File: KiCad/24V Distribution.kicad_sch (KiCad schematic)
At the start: 0 parts

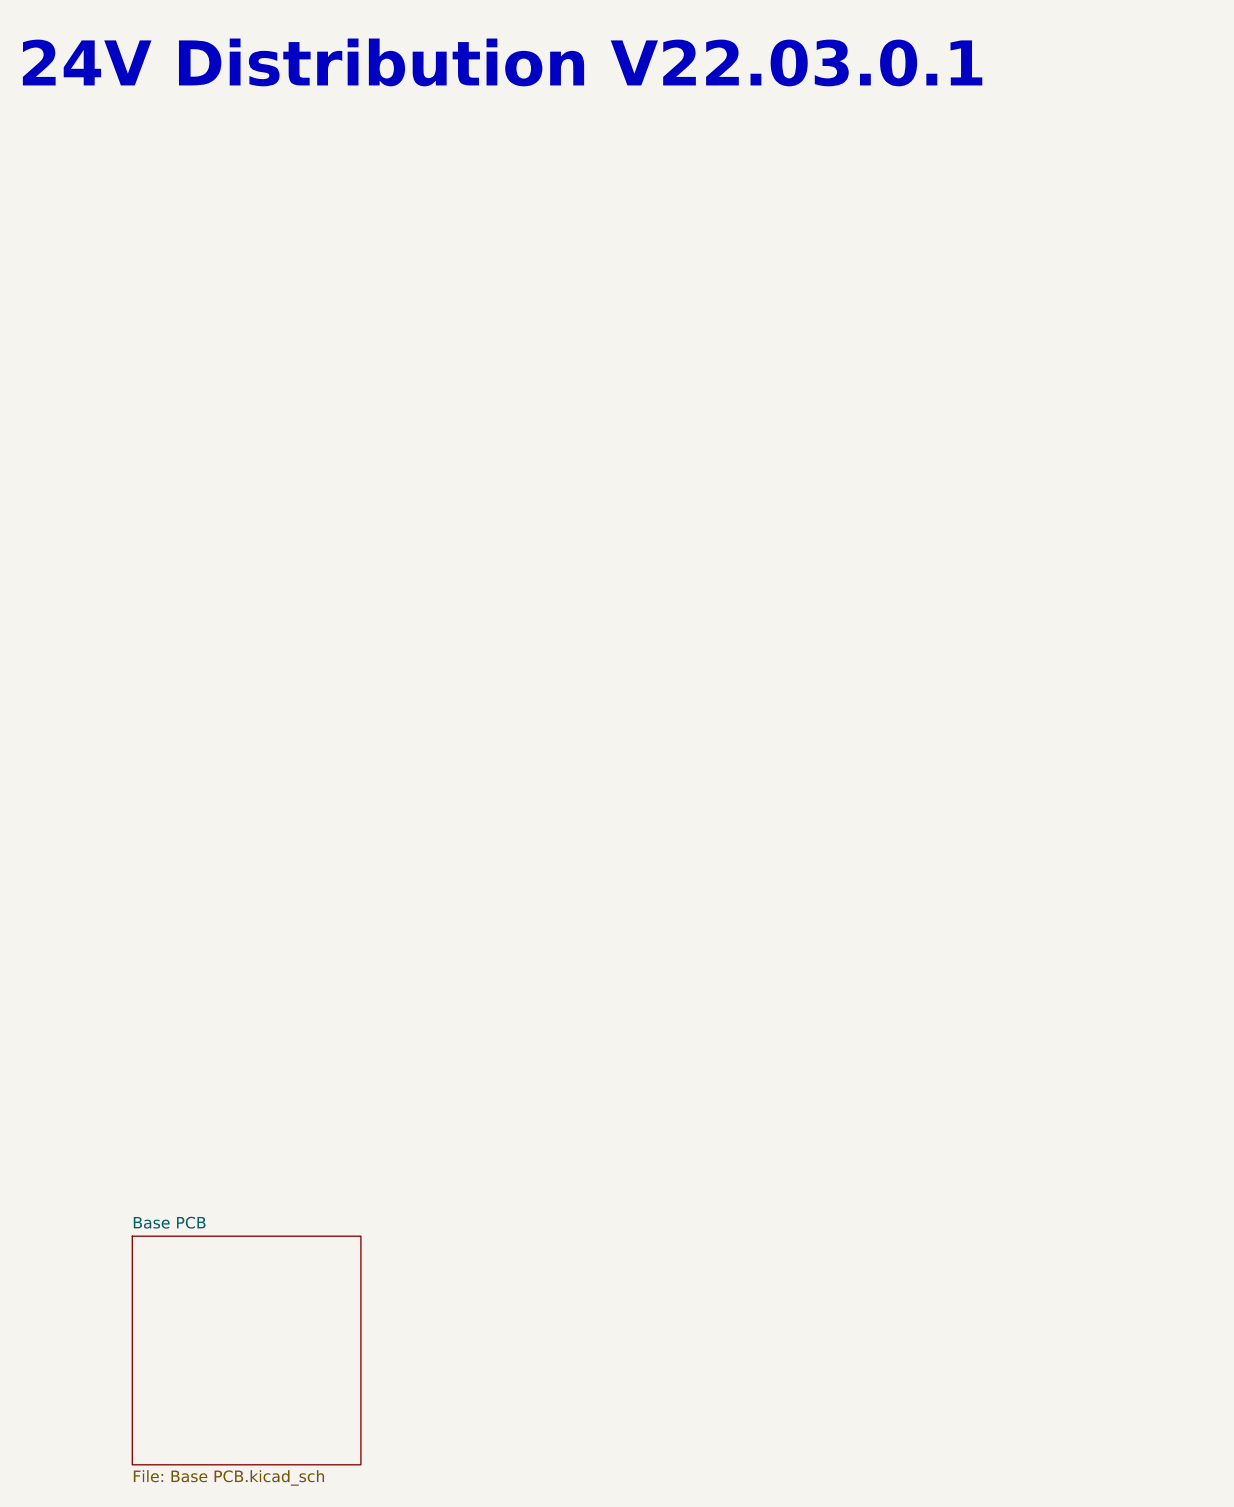
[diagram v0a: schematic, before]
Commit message: Updated PCB and schematic and changed datasheet
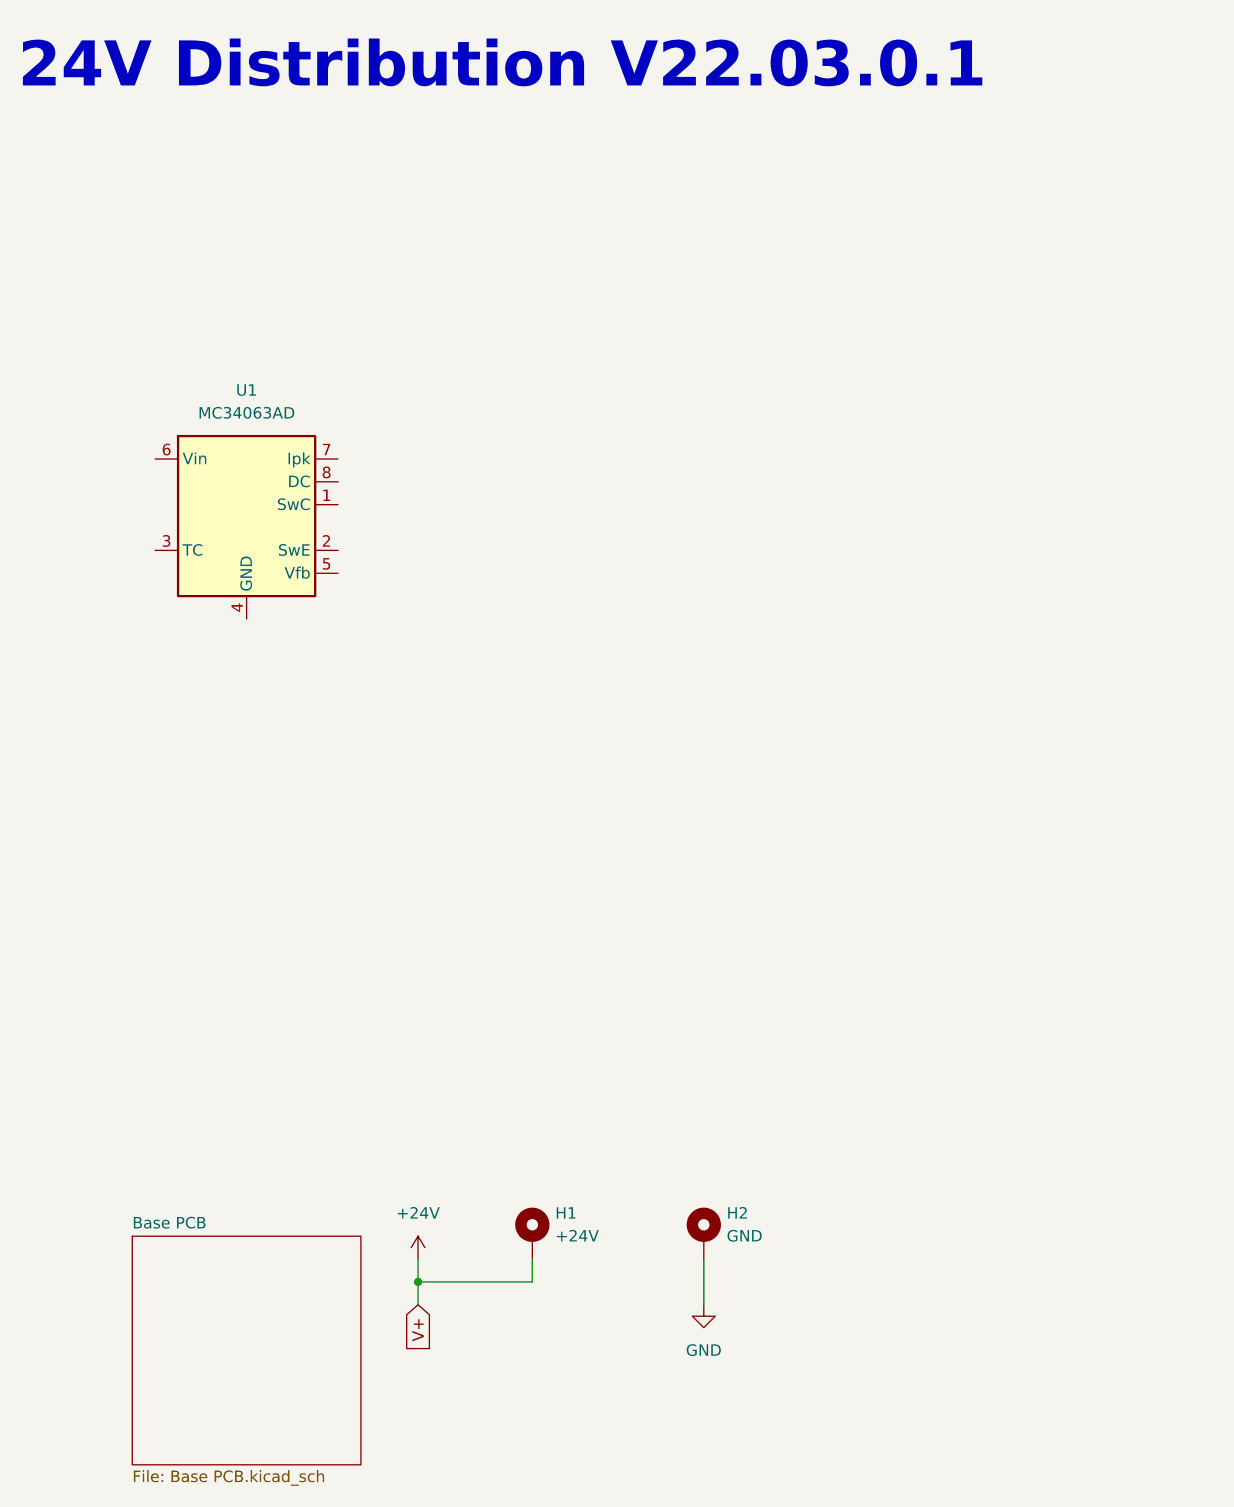
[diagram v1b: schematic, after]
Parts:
- added H1: +24V, MountingHole:MountingHole_4.3mm_M4_Pad_Via, symbol Mechanical:MountingHole_Pad
- added H2: GND, MountingHole:MountingHole_4.3mm_M4_Pad_Via, symbol Mechanical:MountingHole_Pad
- added U1: MC34063AD, Package_SO:SOIC-8_3.9x4.9mm_P1.27mm, symbol Regulator_Switching:MC34063AD
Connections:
- new net +24V: H1.1
- new net GND: H2.1
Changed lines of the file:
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@@
     (rev "V22.03.0.1")
+  )
+  (junction (at 69.85 157.48) (diameter 0) (color 0 0 0 0)
+  )
+  (wire (pts (xy 69.85 157.48) (xy 69.85 160.02))
+    (stroke (width 0) (type default) (color 0 0 0 0))
+  )
+  (wire (pts (xy 101.6 154.94) (xy 101.6 160.02))
+    (stroke (width 0) (type default) (color 0 0 0 0))
+  )
+  (wire (pts (xy 82.55 154.94) (xy 82.55 157.48))
+    (stroke (width 0) (type default) (color 0 0 0 0))
+  )
+  (wire (pts (xy 82.55 157.48) (xy 69.85 157.48))
+    (stroke (width 0) (type default) (color 0 0 0 0))
+  )
+  (wire (pts (xy 69.85 154.94) (xy 69.85 157.48))
+    (stroke (width 0) (type default) (color 0 0 0 0))
   )
   (text "24V Distribution V22.03.0.1" (at 25.4 25.4 0)
     (effects (font (size 5.0038 5.0038) (thickness 1.0008) bold) (justify left bottom))
+  )
+  (global_label "V+" (shape input) (at 69.85 160.02 270) (fields_autoplaced)
+    (effects (font (size 1.27 1.27)) (justify right))
+    (property "Intersheet References" "${INTERSHEET_REFS}" (id 0) (at 69.7706 165.0052 90)
+      (effects (font (size 1.27 1.27)) (justify right) hide)
+    )
+  )
+  (symbol (lib_id "Regulator_Switching:MC34063AD") (at 50.8 71.12 0) (unit 1)
+    (in_bom yes) (on_board yes) (fields_autoplaced)
+    (property "Reference" "U1" (id 0) (at 50.8 58.42 0))
+    (property "Value" "MC34063AD" (id 1) (at 50.8 60.96 0))
+    (property "Footprint" "Package_SO:SOIC-8_3.9x4.9mm_P1.27mm" (id 2) (at 52.07 82.55 0)
+      (effects (font (size 1.27 1.27)) (justify left) hide)
+    )
+    (property "Datasheet" "http://www.onsemi.com/pub_link/Collateral/MC34063A-D.PDF" (id 3) (at 63.5 73.66 0)
+      (effects (font (size 1.27 1.27)) hide)
+    )
+    (pin "1")
+    (pin "2")
+    (pin "3")
+    (pin "4")
+    (pin "5")
+    (pin "6")
+    (pin "7")
+    (pin "8")
+  )
+  (symbol (lib_id "Mechanical:MountingHole_Pad") (at 101.6 152.4 0) (unit 1)
+    (in_bom yes) (on_board yes) (fields_autoplaced)
+    (property "Reference" "H2" (id 0) (at 104.14 149.8599 0)
+      (effects (font (size 1.27 1.27)) (justify left))
+    )
+    (property "Value" "GND" (id 1) (at 104.14 152.3999 0)
+      (effects (font (size 1.27 1.27)) (justify left))
+    )
+    (property "Footprint" "MountingHole:MountingHole_4.3mm_M4_Pad_Via" (id 2) (at 101.6 152.4 0)
+      (effects (font (size 1.27 1.27)) hide)
+    )
+    (property "Datasheet" "~" (id 3) (at 101.6 152.4 0)
+      (effects (font (size 1.27 1.27)) hide)
+    )
+    (pin "1")
+  )
+  (symbol (lib_id "power:GND") (at 101.6 160.02 0) (unit 1)
+    (in_bom yes) (on_board yes) (fields_autoplaced)
+    (property "Reference" "#PWR0101" (id 0) (at 101.6 166.37 0)
+      (effects (font (size 1.27 1.27)) hide)
+    )
+    (property "Value" "GND" (id 1) (at 101.6 165.1 0))
+    (property "Footprint" "" (id 2) (at 101.6 160.02 0)
+      (effects (font (size 1.27 1.27)) hide)
+    )
+    (property "Datasheet" "" (id 3) (at 101.6 160.02 0)
+      (effects (font (size 1.27 1.27)) hide)
+    )
+    (pin "1")
+  )
+  (symbol (lib_id "power:+24V") (at 69.85 154.94 0) (unit 1)
+    (in_bom yes) (on_board yes) (fields_autoplaced)
+    (property "Reference" "#PWR0102" (id 0) (at 69.85 158.75 0)
+      (effects (font (size 1.27 1.27)) hide)
+    )
+    (property "Value" "+24V" (id 1) (at 69.85 149.86 0))
+    (property "Footprint" "" (id 2) (at 69.85 154.94 0)
+      (effects (font (size 1.27 1.27)) hide)
+    )
+    (property "Datasheet" "" (id 3) (at 69.85 154.94 0)
+      (effects (font (size 1.27 1.27)) hide)
+    )
+    (pin "1")
+  )
+  (symbol (lib_id "Mechanical:MountingHole_Pad") (at 82.55 152.4 0) (unit 1)
+    (in_bom yes) (on_board yes) (fields_autoplaced)
+    (property "Reference" "H1" (id 0) (at 85.09 149.8599 0)
+      (effects (font (size 1.27 1.27)) (justify left))
+    )
+    (property "Value" "+24V" (id 1) (at 85.09 152.3999 0)
+      (effects (font (size 1.27 1.27)) (justify left))
+    )
+    (property "Footprint" "MountingHole:MountingHole_4.3mm_M4_Pad_Via" (id 2) (at 82.55 152.4 0)
+      (effects (font (size 1.27 1.27)) hide)
+    )
+    (property "Datasheet" "~" (id 3) (at 82.55 152.4 0)
+      (effects (font (size 1.27 1.27)) hide)
+    )
+    (pin "1")
   )
   (sheet (at 38.1 152.4) (size 25.4 25.4) (fields_autoplaced)
@@
   )
   (symbol_instances
+    (path "/a6944de9-4199-43c7-a2d8-2f045cf8e8df"
+      (reference "#PWR0101") (unit 1) (value "GND") (footprint "")
+    )
+    (path "/a6fd9401-e35c-44ed-9fc2-309b0dfcea83"
+      (reference "#PWR0102") (unit 1) (value "+24V") (footprint "")
+    )
     (path "/00000000-0000-0000-0000-000061aa1a42/00000000-0000-0000-0000-000061abb3c4"
       (reference "#PWR0201") (unit 1) (value "GND") (footprint "")
@@
     (path "/00000000-0000-0000-0000-000061aa1a42/00000000-0000-0000-0000-000061abb3bc"
       (reference "GND201") (unit 1) (value "Scope GND") (footprint "MEP_TEMPLATE:Scope_GND")
+    )
+    (path "/f487808c-3e4e-41c4-a1f4-b02337ae2310"
+      (reference "H1") (unit 1) (value "+24V") (footprint "MountingHole:MountingHole_4.3mm_M4_Pad_Via")
+    )
+    (path "/3a49d270-f8e5-4823-86ca-a16b53f0af62"
+      (reference "H2") (unit 1) (value "GND") (footprint "MountingHole:MountingHole_4.3mm_M4_Pad_Via")
     )
     (path "/00000000-0000-0000-0000-000061aa1a42/00000000-0000-0000-0000-000061abb3dc"
@@
       (reference "JP201") (unit 1) (value "GND Jumper") (footprint "TestPoint:TestPoint_2Pads_Pitch2.54mm_Drill0.8mm")
     )
+    (path "/0023162f-a07e-408b-b318-1e8e9f305001"
+      (reference "U1") (unit 1) (value "MC34063AD") (footprint "Package_SO:SOIC-8_3.9x4.9mm_P1.27mm")
+    )
   )
